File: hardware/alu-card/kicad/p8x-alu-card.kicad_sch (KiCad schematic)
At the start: 0 parts

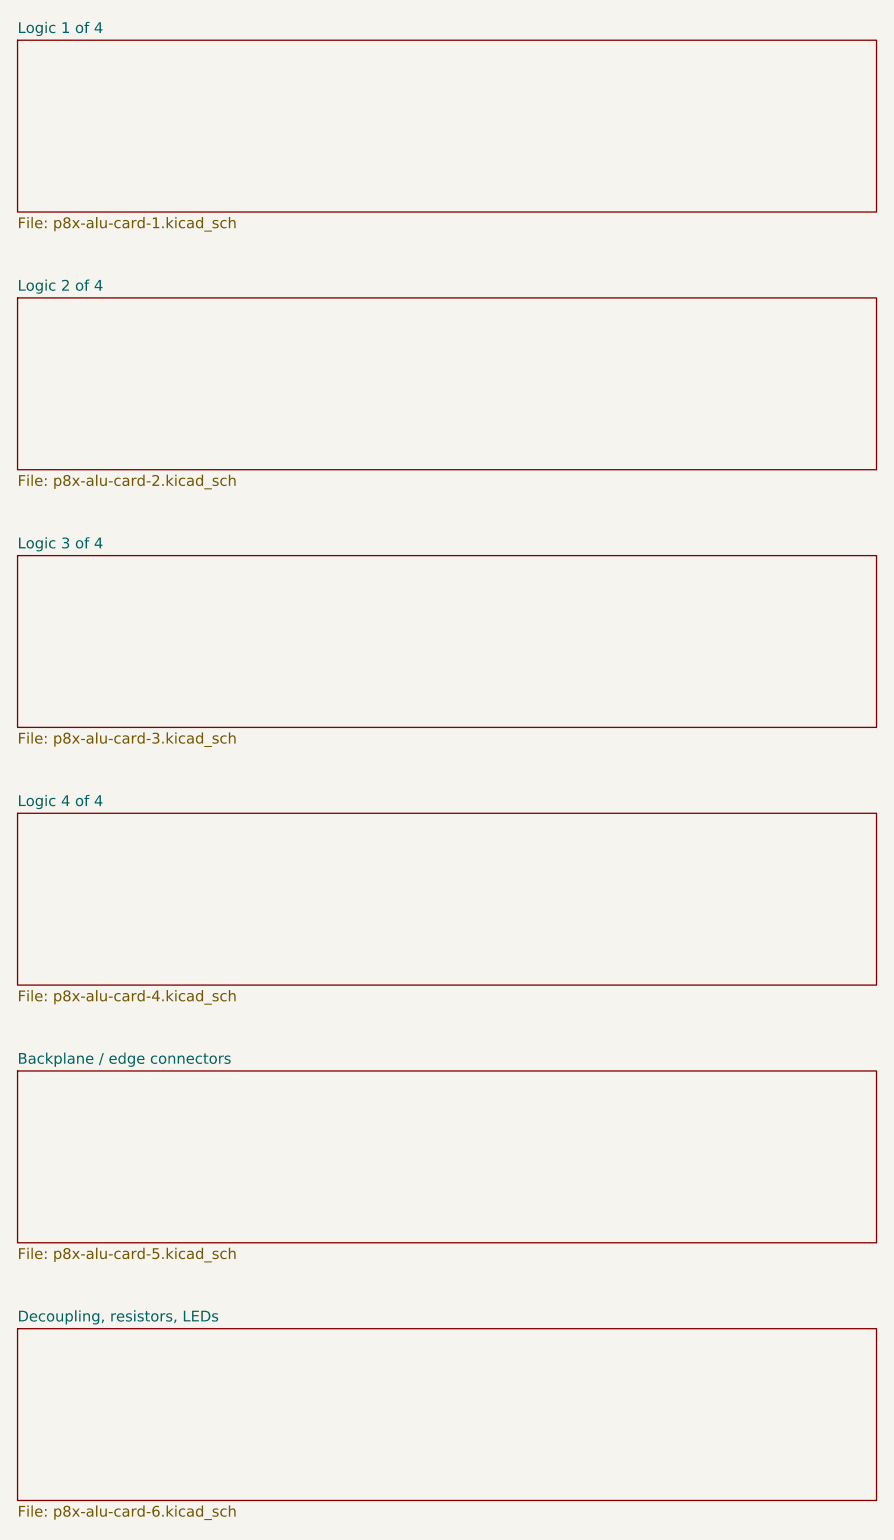
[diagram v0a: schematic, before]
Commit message: feat(sch): draw every P8X card schematic by function
Extend the functional-sheet grouping from the io-card to the control,
regbank, alu, memory, cf, ps2 and bustest cards. functional_sheets now
attaches unnamed glue gates, LEDs, resistors and connectors to the block
they share the most local nets with, so each block lists only its main
parts. A net with two or more pins on a sheet is now wired there even if
it continues elsewhere (its global name label rides on the wire), and
every wire is oriented by drawing side. The regbank gets one pointer per
sheet; the ps2 latches share a sheet with the AVR so the mailbox bus is
drawn. The bustest probe resistors use a straight-order RNISO8DSTR
drawing (the reversed B side forced every wire to cross and the sheet
fell back to labels). build_sch.sh now shows ELK fallbacks and clears old
numbered sheets before a build. All eight netlists match the boards,
ERC 0 errors; the boards change only in footprint link paths.

Co-Authored-By: Claude Opus 5.5 <noreply@anthropic.com>
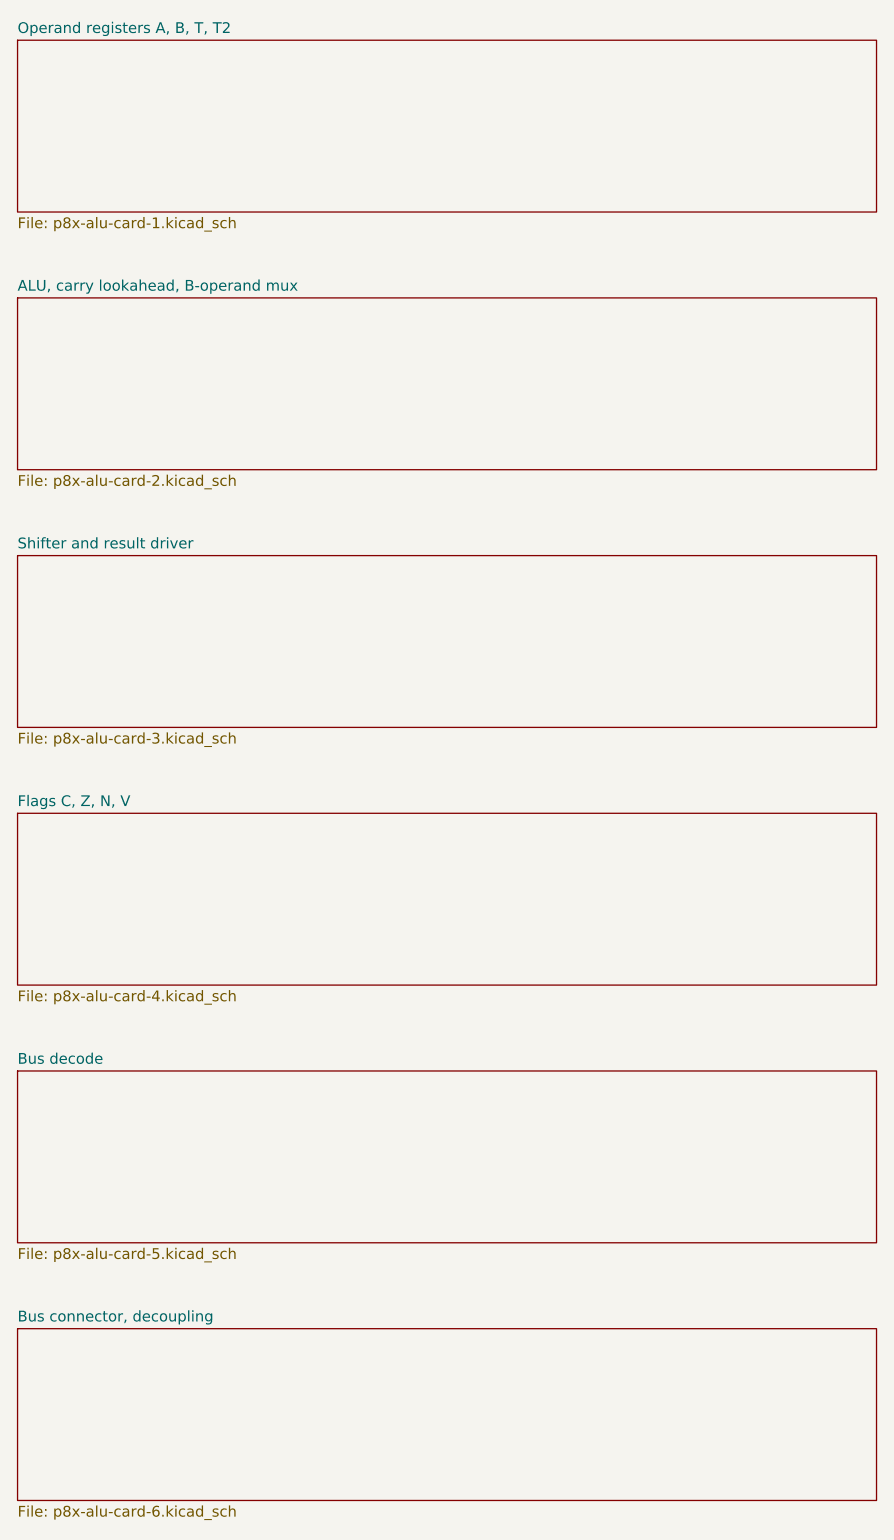
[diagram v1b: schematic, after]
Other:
- sheet Backplane / edge connectors renamed Bus decode
- sheet Decoupling, resistors, LEDs renamed Bus connector, decoupling
- sheet Logic 1 of 4 renamed Operand registers A, B, T, T2
- sheet Logic 2 of 4 renamed ALU, carry lookahead, B-operand mux
- sheet Logic 3 of 4 renamed Shifter and result driver
- sheet Logic 4 of 4 renamed Flags C, Z, N, V
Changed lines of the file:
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@@
   (sheet (at 25.40 30.48) (size 101.6 20.32) (fields_autoplaced yes)
     (stroke (width 0.1524) (type solid)) (fill (color 0 0 0 0.0000))
-    (property "Sheetname" "Logic 1 of 4" (at 25.40 29.78 0) (effects (font (size 1.27 1.27)) (justify left bottom)))
+    (property "Sheetname" "Operand registers A, B, T, T2" (at 25.40 29.78 0) (effects (font (size 1.27 1.27)) (justify left bottom)))
     (property "Sheetfile" "p8x-alu-card-1.kicad_sch" (at 25.40 51.38 0) (effects (font (size 1.27 1.27)) (justify left top)))
     (instances (project "p8x-alu-card" (path "/59f264d2-36c6-5d57-bdbb-67a74f30b681" (page "2"))))
@@
   (sheet (at 25.40 60.96) (size 101.6 20.32) (fields_autoplaced yes)
     (stroke (width 0.1524) (type solid)) (fill (color 0 0 0 0.0000))
-    (property "Sheetname" "Logic 2 of 4" (at 25.40 60.26 0) (effects (font (size 1.27 1.27)) (justify left bottom)))
+    (property "Sheetname" "ALU, carry lookahead, B-operand mux" (at 25.40 60.26 0) (effects (font (size 1.27 1.27)) (justify left bottom)))
     (property "Sheetfile" "p8x-alu-card-2.kicad_sch" (at 25.40 81.86 0) (effects (font (size 1.27 1.27)) (justify left top)))
     (instances (project "p8x-alu-card" (path "/59f264d2-36c6-5d57-bdbb-67a74f30b681" (page "3"))))
@@
   (sheet (at 25.40 91.44) (size 101.6 20.32) (fields_autoplaced yes)
     (stroke (width 0.1524) (type solid)) (fill (color 0 0 0 0.0000))
-    (property "Sheetname" "Logic 3 of 4" (at 25.40 90.74 0) (effects (font (size 1.27 1.27)) (justify left bottom)))
+    (property "Sheetname" "Shifter and result driver" (at 25.40 90.74 0) (effects (font (size 1.27 1.27)) (justify left bottom)))
     (property "Sheetfile" "p8x-alu-card-3.kicad_sch" (at 25.40 112.34 0) (effects (font (size 1.27 1.27)) (justify left top)))
     (instances (project "p8x-alu-card" (path "/59f264d2-36c6-5d57-bdbb-67a74f30b681" (page "4"))))
@@
   (sheet (at 25.40 121.92) (size 101.6 20.32) (fields_autoplaced yes)
     (stroke (width 0.1524) (type solid)) (fill (color 0 0 0 0.0000))
-    (property "Sheetname" "Logic 4 of 4" (at 25.40 121.22 0) (effects (font (size 1.27 1.27)) (justify left bottom)))
+    (property "Sheetname" "Flags C, Z, N, V" (at 25.40 121.22 0) (effects (font (size 1.27 1.27)) (justify left bottom)))
     (property "Sheetfile" "p8x-alu-card-4.kicad_sch" (at 25.40 142.82 0) (effects (font (size 1.27 1.27)) (justify left top)))
     (instances (project "p8x-alu-card" (path "/59f264d2-36c6-5d57-bdbb-67a74f30b681" (page "5"))))
@@
   (sheet (at 25.40 152.40) (size 101.6 20.32) (fields_autoplaced yes)
     (stroke (width 0.1524) (type solid)) (fill (color 0 0 0 0.0000))
-    (property "Sheetname" "Backplane / edge connectors" (at 25.40 151.70 0) (effects (font (size 1.27 1.27)) (justify left bottom)))
+    (property "Sheetname" "Bus decode" (at 25.40 151.70 0) (effects (font (size 1.27 1.27)) (justify left bottom)))
     (property "Sheetfile" "p8x-alu-card-5.kicad_sch" (at 25.40 173.30 0) (effects (font (size 1.27 1.27)) (justify left top)))
     (instances (project "p8x-alu-card" (path "/59f264d2-36c6-5d57-bdbb-67a74f30b681" (page "6"))))
@@
   (sheet (at 25.40 182.88) (size 101.6 20.32) (fields_autoplaced yes)
     (stroke (width 0.1524) (type solid)) (fill (color 0 0 0 0.0000))
-    (property "Sheetname" "Decoupling, resistors, LEDs" (at 25.40 182.18 0) (effects (font (size 1.27 1.27)) (justify left bottom)))
+    (property "Sheetname" "Bus connector, decoupling" (at 25.40 182.18 0) (effects (font (size 1.27 1.27)) (justify left bottom)))
     (property "Sheetfile" "p8x-alu-card-6.kicad_sch" (at 25.40 203.78 0) (effects (font (size 1.27 1.27)) (justify left top)))
     (instances (project "p8x-alu-card" (path "/59f264d2-36c6-5d57-bdbb-67a74f30b681" (page "7"))))
